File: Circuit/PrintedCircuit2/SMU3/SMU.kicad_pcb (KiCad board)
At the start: 2 copper layers, 100 x 83 mm, 49 parts, among them J1 Conn_Coaxial, J2 Conn_Coaxial, SW1 SW_SPDT, SW2 SW_SPDT, U1 TPS65131_kit, U10 OP07, U11 OP07, U2 MCP1501-20xCH, U3 MCP4922, U6 TLP241AF, U7 TLP241AF, U8 OP07, U9 OP07

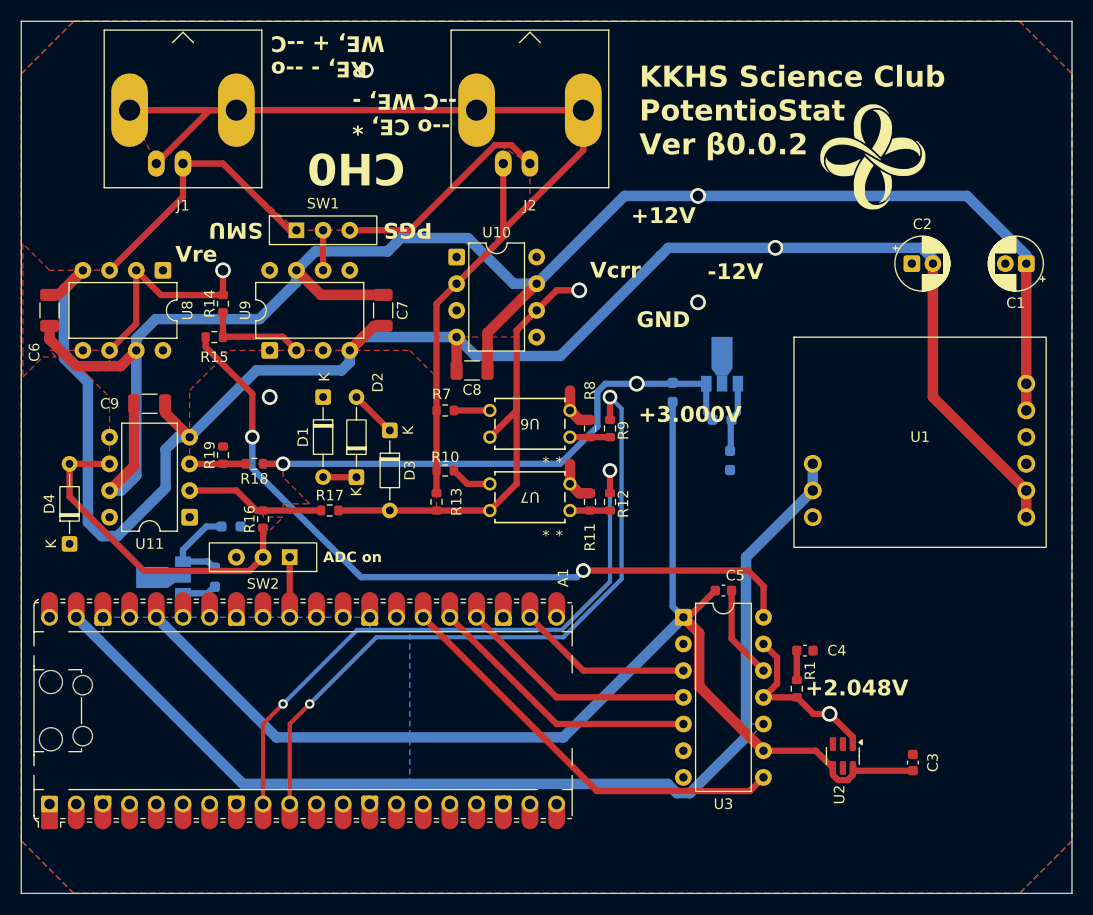
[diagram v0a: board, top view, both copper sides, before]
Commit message: 実装を表に集中
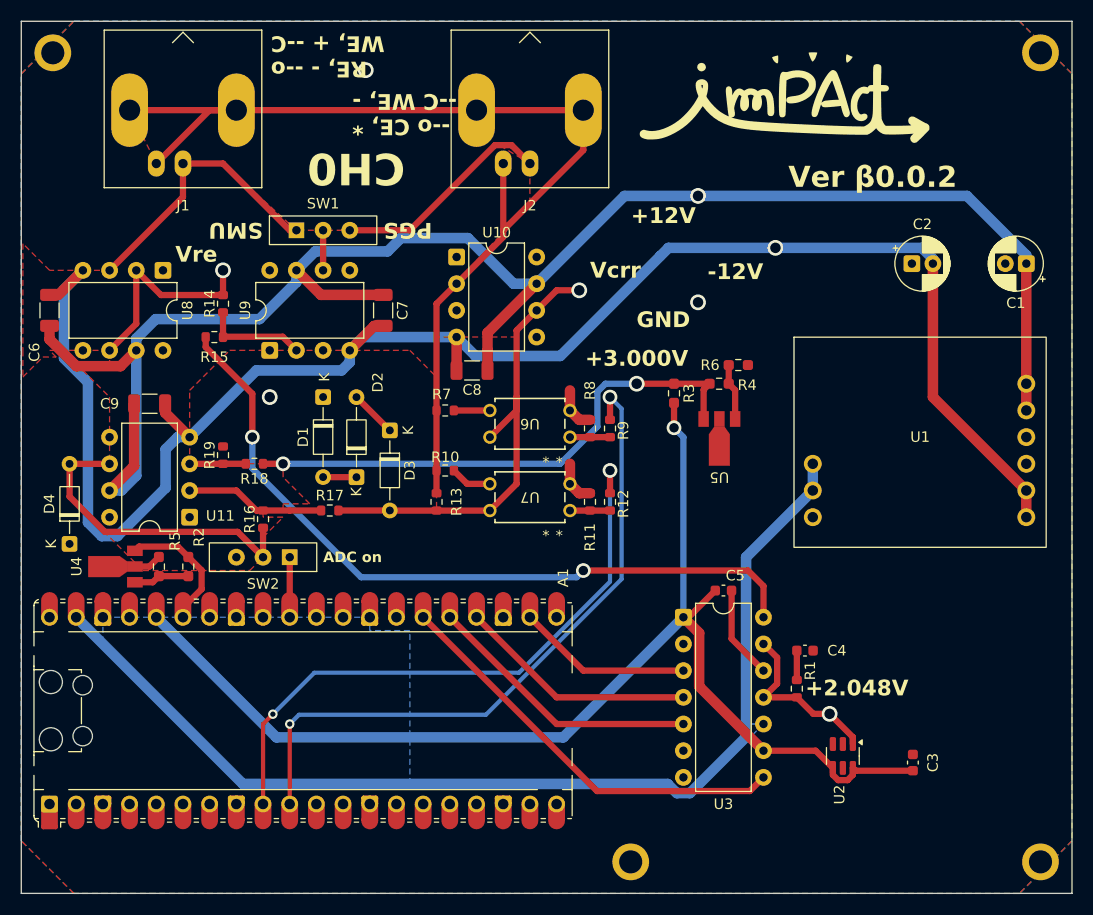
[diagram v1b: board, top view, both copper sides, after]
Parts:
- added ?: , , F.Cu at (83.0, 196.0)
- added REF**: MountingHole_2.2mm_M2_ISO7380_Pad, MountingHole:MountingHole_2.2mm_M2_ISO7380_Pad, F.Cu at (122.0, 196.0)
- added REF**: MountingHole_2.2mm_M2_ISO7380_Pad, MountingHole:MountingHole_2.2mm_M2_ISO7380_Pad, F.Cu at (28.0, 119.0)
- added REF**: MountingHole_2.2mm_M2_ISO7380_Pad, MountingHole:MountingHole_2.2mm_M2_ISO7380_Pad, F.Cu at (122.0, 119.0)
- R2, R3, R4, R5, R6, U4, U5: moved to F.Cu
- moved G*** 9.42 mm to (98.0, 124.0)
- moved R6 9.11 mm to (93.2, 148.7), turned to 180 degrees
- moved R5 7.85 mm to (38.1, 167.9), turned to -90 degrees
- moved U4 4.69 mm to (35.8, 167.9), turned to 90 degrees
- moved R4 3.44 mm to (91.4, 150.5)
- moved U5 3.36 mm to (91.4, 153.8)
- moved R2 2.74 mm to (40.9, 167.9), turned to -90 degrees
- moved R3 0.15 mm to (87.1, 151.4)
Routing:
- net Net-(A1-ADC_VREF): track 5.63 -> 11.9 mm
- net Net-(U4-REF): track 9.12 -> 5.32 mm
- net GND: track 17.2 -> 19.9 mm
- net /反転回路/OUTPUT: track 31.6 -> 30.5 mm
- net Net-(U5-REF): track 6.40 -> 5.39 mm
- net 3.0V_REF: track 50.8 -> 51.4 mm
- net +3.3V: track 117.3 -> 117.1 mm, vias 0 -> 1
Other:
- board text added: "Ver β0.0.2"
- board text removed: "KKHS Science Club PotentioStat Ver β0.0.2"

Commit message: 3Dモデルを更新
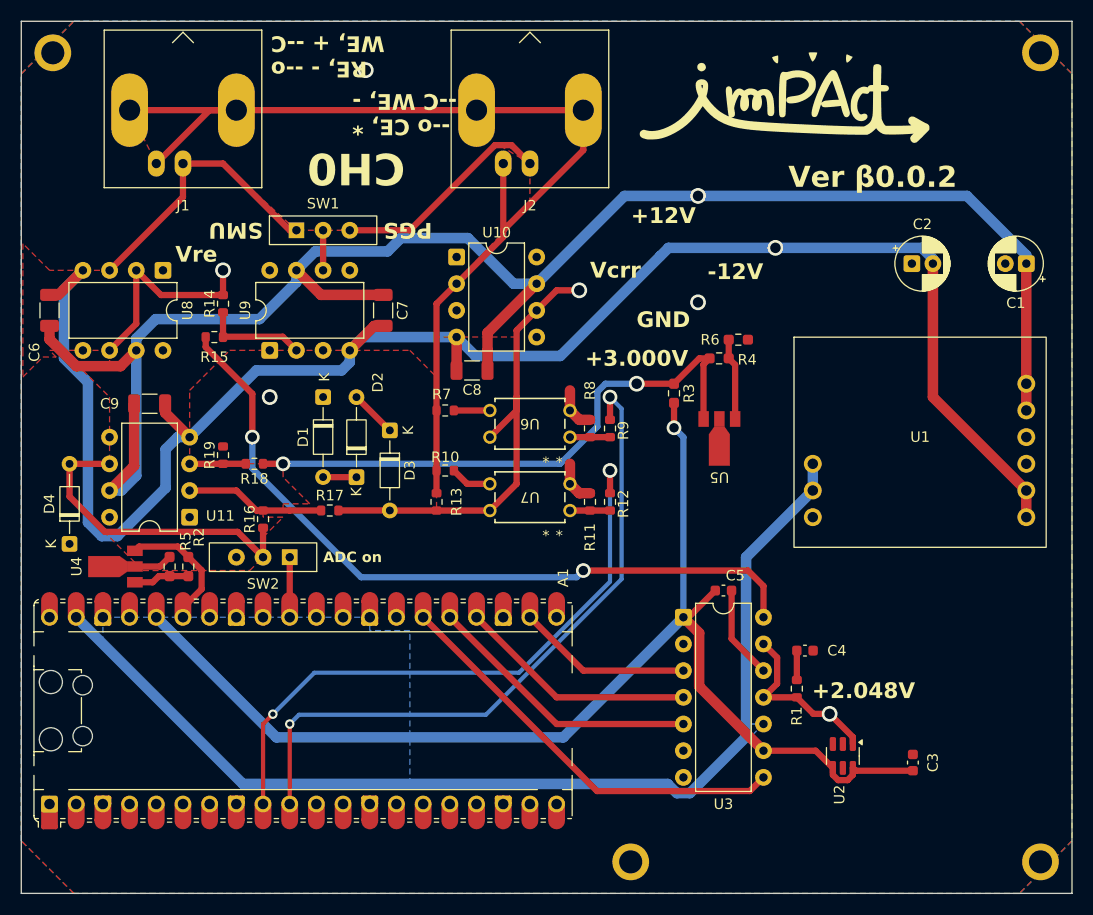
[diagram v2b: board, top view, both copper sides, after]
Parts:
- moved R4 2.41 mm to (91.4, 148.1)
- moved R6 2.41 mm to (93.2, 146.3)
- moved R5 1.02 mm to (39.1, 167.9)
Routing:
- net 3.0V_REF: track 51.4 -> 54.8 mm
- net Net-(U5-REF): track 5.39 -> 7.80 mm
- net GND: track 19.9 -> 20.9 mm

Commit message: β0.0.3
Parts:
- removed ?: , 
- removed REF** (x3): MountingHole_2.2mm_M2_ISO7380_Pad, MountingHole:MountingHole_2.2mm_M2_ISO7380_Pad
- added R6: 51, Resistor_SMD:R_0603_1608Metric, F.Cu at (41.3, 167.1)
- R10: renamed from R8; value 10k -> 4.7k
- R11: renamed from R9; value 20k -> 8.2k
- R12: renamed from R13; value 100 -> 10k
- R13: renamed from R11; value 10k -> 4.7k
- R15: renamed from R12; value 20k -> 8.2k
- R2, R4: value 10 -> 1k; footprint Resistor_SMD:R_0603_1608Metric_Pad0.98x0.95mm_HandSolder -> Resistor_SMD:R_0603_1608Metric
- R3: value 50 -> 51; footprint Resistor_SMD:R_0603_1608Metric_Pad0.98x0.95mm_HandSolder -> Resistor_SMD:R_0603_1608Metric
- R5: value 50 -> 5.1k; footprint Resistor_SMD:R_0603_1608Metric_Pad0.98x0.95mm_HandSolder -> Resistor_SMD:R_0603_1608Metric
- R7: renamed from R6; value 50 -> 5.1k; footprint Resistor_SMD:R_0603_1608Metric_Pad0.98x0.95mm_HandSolder -> Resistor_SMD:R_0603_1608Metric
- R8: renamed from R7; value 10k -> 100
- moved D4 3.81 mm to (29.6, 161.9)
- moved R17 3.32 mm to (51.3, 163.8)
- moved SW2 3.32 mm to (51.3, 167.4)
- moved U4 2.46 mm to (34.3, 166.0)
- moved R2 2.44 mm to (41.3, 165.5), turned to 180 degrees
- moved R19 2.10 mm to (45.1, 158.1)
- moved R5 2.00 mm to (37.6, 166.6)
- moved C9 1.91 mm to (37.2, 150.5)
- moved U11 1.91 mm to (41.0, 161.3)
- moved R20 1.91 mm to (44.2, 155.4)
- renumbered R15 to R16, R16 to R17, R17 to R18, R18 to R19, R19 to R20, R10 to R9, U8 to U7, U7 to U8
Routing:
- net +3.3V: track 117.1 -> 122.9 mm
- net /反転回路/OUTPUT: track 30.5 -> 36.3 mm
- net Net-(A1-ADC_VREF): track 11.9 -> 15.5 mm
- net +12V: track 167.7 -> 165.2 mm
- net 3.0V_REF: track 54.8 -> 56.9 mm
- net Net-(U4-REF): track 5.32 -> 6.93 mm
- net Net-(A1-GPIO26_ADC0): track 4.91 -> 5.90 mm
- net Net-(U11--): track 13.3 -> 14.1 mm
- net /PotentioStatUnit/INPUT: track 71.1 -> 70.6 mm
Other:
- board text added: "Ver β0.0.3"
- board text removed: "Ver β0.0.2"

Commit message: 保護回路を変更
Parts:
- added D2: D, Diode_THT:D_DO-34_SOD68_P2.54mm_Vertical_KathodeUp, F.Cu at (26.8, 161.4)
- added D3: D, Diode_THT:D_DO-34_SOD68_P2.54mm_Vertical_KathodeUp, F.Cu at (26.8, 156.2)
- added D5: D, Diode_THT:D_DO-34_SOD68_P2.54mm_Vertical_KathodeUp, F.Cu at (29.3, 153.7)
- D1: footprint Diode_THT:D_DO-34_SOD68_P7.62mm_Horizontal -> Diode_THT:D_DO-34_SOD68_P2.54mm_Vertical_KathodeUp
- D4: value ZeD -> D; footprint Diode_THT:D_DO-34_SOD68_P7.62mm_Horizontal -> Diode_THT:D_DO-34_SOD68_P2.54mm_Vertical_KathodeUp
- D6: renamed from D2; footprint Diode_THT:D_DO-34_SOD68_P7.62mm_Horizontal -> Diode_THT:D_DO-34_SOD68_P2.54mm_Vertical_KathodeUp
- D7: renamed from D3; footprint Diode_THT:D_DO-34_SOD68_P7.62mm_Horizontal -> Diode_THT:D_DO-34_SOD68_P2.54mm_Vertical_KathodeUp
- moved D1 30.7 mm to (26.8, 166.5), turned to 90 degrees
- moved D4 11.3 mm to (26.8, 151.0), turned to 0 degrees
- moved D6 5.47 mm to (52.5, 156.2), turned to 0 degrees
- moved D7 2.85 mm to (57.5, 156.2), turned to 0 degrees
- renumbered C5 to C4, C4 to C5, C7 to C6, C6 to C7, R6 to R1, R8 to R10, R9 to R11, R10 to R13, R13 to R14, R11 to R15, R15 to R16, R19 to R18, R18 to R19, R5 to R3, R1 to R4, R3 to R5, R4 to R6, R16 to R8, R14 to R9, SW2 to SW1, SW1 to SW2, U8 to U10, U4 to U2, U2 to U3, U3 to U4, U9 to U6, U10 to U8, U6 to U9
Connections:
- D4 pad 1: GND -> Net-(D3-A)
- D4 pad 2: /反転回路/OUTPUT -> Net-(D4-A)
- D6 pad 1: Net-(D1-A) -> GND
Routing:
- net /PotentioStatUnit/Vcrr: track 45.0 -> 51.4 mm
- net /反転回路/OUTPUT: track 36.3 -> 33.4 mm
- net Net-(D4-A): track 0.00 -> 2.67 mm
- net Net-(D3-A): track 0.00 -> 2.67 mm
- net Net-(D2-A): track 0.00 -> 2.65 mm
- net Net-(D6-A): track 4.49 -> 2.54 mm
- net Net-(D1-A): track 3.16 -> 2.56 mm
